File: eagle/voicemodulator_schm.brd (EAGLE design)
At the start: 109 x 84 mm, 33 parts, among them T1 2N5089, T2 2N5089, T3 2N5089, T4 2N5089

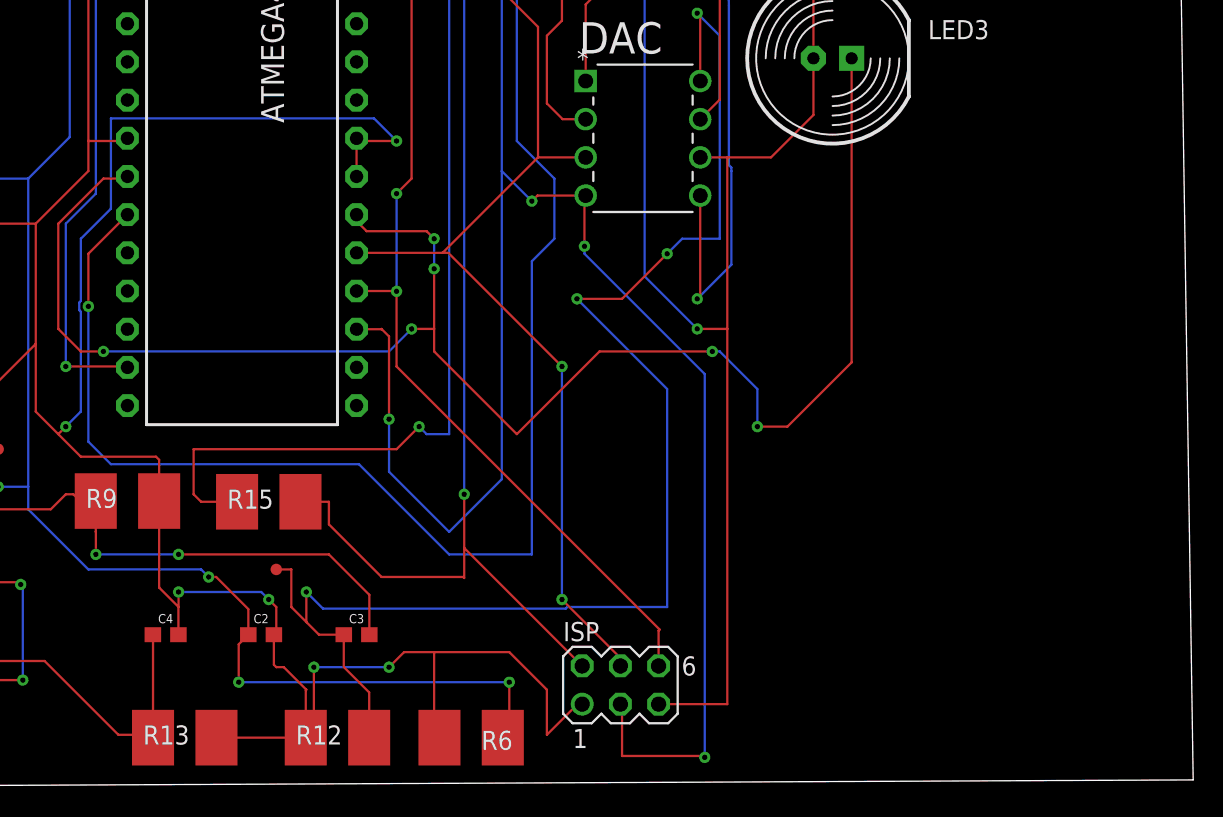
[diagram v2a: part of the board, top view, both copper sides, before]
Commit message: Added output mic jack.
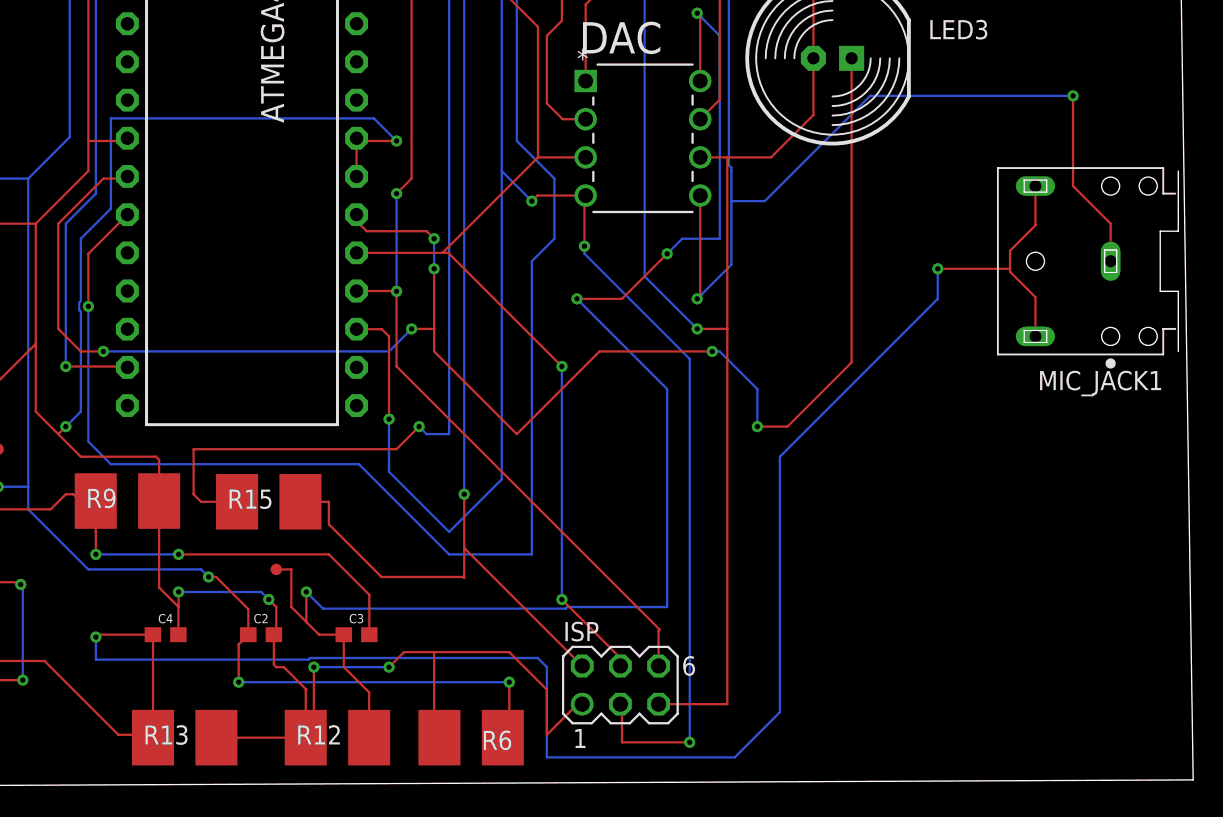
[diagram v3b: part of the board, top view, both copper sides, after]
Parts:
- added MIC_JACK1: SJ1-3523N, SJ1-3523N:CUI_SJ1-3523N
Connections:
- net 0: now also MIC_JACK1.1
- net N$11: now also MIC_JACK1.2, MIC_JACK1.3
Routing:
- net N$11: track 26.9 -> 135.3 mm, vias 0 -> 2
- net 0: track 359.8 -> 397.4 mm, vias 12 -> 13
- net N$16: track 146.3 -> 142.9 mm
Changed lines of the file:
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@@
 <attribute name="VALUE" x="91.35" y="47.23" size="1.27" layer="27"/>
+</element>
+<element name="MIC_JACK1" library="SJ1-3523N" package="CUI_SJ1-3523N" value="SJ1-3523N" x="103.5" y="35" rot="R180">
+<attribute name="MANUFACTURER" value="CUI" x="103.5" y="35" size="1.778" layer="27" rot="R180" display="off"/>
+<attribute name="NAME" x="107.001409375" y="27.69706875" size="1.270509375" layer="25" rot="R180"/>
+<attribute name="PARTREV" value="1.02" x="103.5" y="35" size="1.778" layer="27" rot="R180" display="off"/>
+<attribute name="STANDARD" value="Manufacturer recommendation" x="103.5" y="35" size="1.778" layer="27" rot="R180" display="off"/>
+<attribute name="VALUE" x="107.00286875" y="42.005740625" size="1.271040625" layer="27" rot="R180" align="top-left"/>
 </element>
 </elements>
@@
 <wire x1="78.106771875" y1="41.393228125" x2="78.270515625" y2="41.229484375" width="0.1524" layer="16"/>
 <wire x1="78.270515625" y1="41.229484375" x2="78.274059375" y2="40.9965625" width="0.1524" layer="16"/>
-<wire x1="78.274059375" y1="40.9965625" x2="78.274059375" y2="34.774059375" width="0.1524" layer="16"/>
+<wire x1="78.274059375" y1="40.9965625" x2="78.274059375" y2="39" width="0.1524" layer="16"/>
+<wire x1="78.274059375" y1="39" x2="78.274059375" y2="34.774059375" width="0.1524" layer="16"/>
 <wire x1="78.274059375" y1="34.774059375" x2="76" y2="32.5" width="0.1524" layer="16"/>
 <via x="76" y="32.5" extent="1-16" drill="0.35"/>
@@
 <wire x1="55.5" y1="8" x2="56.5" y2="9" width="0.1524" layer="1"/>
 <wire x1="56.5" y1="9" x2="58.5" y2="9" width="0.1524" layer="1"/>
+<contactref element="MIC_JACK1" pad="1"/>
+<wire x1="103.5" y1="35" x2="103.5" y2="37.5" width="0.1524" layer="1"/>
+<wire x1="101" y1="40" x2="101" y2="46" width="0.1524" layer="1"/>
+<wire x1="103.5" y1="37.5" x2="101" y2="40" width="0.1524" layer="1"/>
+<via x="101" y="46" extent="1-16" drill="0.35"/>
+<wire x1="101" y1="46" x2="87.5" y2="46" width="0.1524" layer="16"/>
+<wire x1="87.5" y1="46" x2="80.5" y2="39" width="0.1524" layer="16"/>
+<wire x1="80.5" y1="39" x2="78.274059375" y2="39" width="0.1524" layer="16"/>
 </signal>
 <signal name="N$1">
@@
 <wire x1="37.5" y1="3.5" x2="39.8018" y2="3.5" width="0.1524" layer="1"/>
 <wire x1="32.59" y1="8.41" x2="37.5" y2="3.5" width="0.1524" layer="1"/>
+<contactref element="MIC_JACK1" pad="3"/>
+<contactref element="MIC_JACK1" pad="2"/>
+<wire x1="96.8078" y1="34.2990625" x2="96.8078" y2="34.5" width="0.1524" layer="1"/>
+<wire x1="96.8078" y1="34.5" x2="96.8078" y2="35.7009375" width="0.1524" layer="1"/>
+<wire x1="98.5" y1="30" x2="98.5" y2="32.6068625" width="0.1524" layer="1"/>
+<wire x1="98.5" y1="37.3931375" x2="98.5" y2="40" width="0.1524" layer="1"/>
+<wire x1="98.5" y1="32.6068625" x2="96.8078" y2="34.2990625" width="0.1524" layer="1"/>
+<wire x1="96.8078" y1="35.7009375" x2="98.5" y2="37.3931375" width="0.1524" layer="1"/>
+<wire x1="39.79" y1="10.16" x2="36.16" y2="10.16" width="0.1524" layer="1"/>
+<wire x1="36.16" y1="10.16" x2="36" y2="10" width="0.1524" layer="1"/>
+<via x="36" y="10" extent="1-16" drill="0.35"/>
+<wire x1="36" y1="10" x2="36" y2="8.5" width="0.1524" layer="16"/>
+<wire x1="36" y1="8.5" x2="50.14185" y2="8.5" width="0.1524" layer="16"/>
+<wire x1="50.14185" y1="8.5" x2="50.24865" y2="8.6068" width="0.1524" layer="16"/>
+<wire x1="50.24865" y1="8.6068" x2="65.3932" y2="8.6068" width="0.1524" layer="16"/>
+<wire x1="65.3932" y1="8.6068" x2="66" y2="8" width="0.1524" layer="16"/>
+<wire x1="66" y1="8" x2="66" y2="2" width="0.1524" layer="16"/>
+<wire x1="66" y1="2" x2="78.5" y2="2" width="0.1524" layer="16"/>
+<wire x1="78.5" y1="2" x2="81.5" y2="5" width="0.1524" layer="16"/>
+<wire x1="81.5" y1="5" x2="81.5" y2="22" width="0.1524" layer="16"/>
+<wire x1="81.5" y1="22" x2="92" y2="32.5" width="0.1524" layer="16"/>
+<wire x1="92" y1="32.5" x2="92" y2="34.5" width="0.1524" layer="16"/>
+<via x="92" y="34.5" extent="1-16" drill="0.35"/>
+<wire x1="92" y1="34.5" x2="96.8078" y2="34.5" width="0.1524" layer="1"/>
 </signal>
 <signal name="N$12">
@@
 <wire x1="65.37" y1="39.37" x2="65" y2="39" width="0.1524" layer="1"/>
 <wire x1="71" y1="5.43" x2="70.89" y2="5.54" width="0.1524" layer="1"/>
-<wire x1="71" y1="5.43" x2="71" y2="2.0922" width="0.1524" layer="1"/>
-<wire x1="76.5" y1="2" x2="76.4078" y2="2.0922" width="0.1524" layer="1"/>
-<wire x1="76.4078" y1="2.0922" x2="71" y2="2.0922" width="0.1524" layer="1"/>
-<via x="76.5" y="2" extent="1-16" drill="0.35"/>
-<wire x1="76.5" y1="27.5" x2="76.5" y2="2" width="0.1524" layer="16"/>
-<wire x1="76.5" y1="27.5" x2="68.5" y2="35.5" width="0.1524" layer="16"/>
+<wire x1="71" y1="5.43" x2="71" y2="3" width="0.1524" layer="1"/>
+<wire x1="75.5" y1="28.5" x2="75.5" y2="3" width="0.1524" layer="16"/>
+<wire x1="75.5" y1="28.5" x2="68.5" y2="35.5" width="0.1524" layer="16"/>
 <wire x1="68.5" y1="35.5" x2="68.5" y2="36" width="0.1524" layer="16"/>
 <via x="68.5" y="36" extent="1-16" drill="0.35"/>
@@
 <wire x1="55" y1="30.5" x2="54.98" y2="30.48" width="0.1524" layer="1"/>
 <wire x1="54.98" y1="30.48" x2="53.34" y2="30.48" width="0.1524" layer="1"/>
+<via x="75.5" y="3" extent="1-16" drill="0.35"/>
+<wire x1="75.5" y1="3" x2="71" y2="3" width="0.1524" layer="1"/>
 </signal>
 <signal name="N$17">

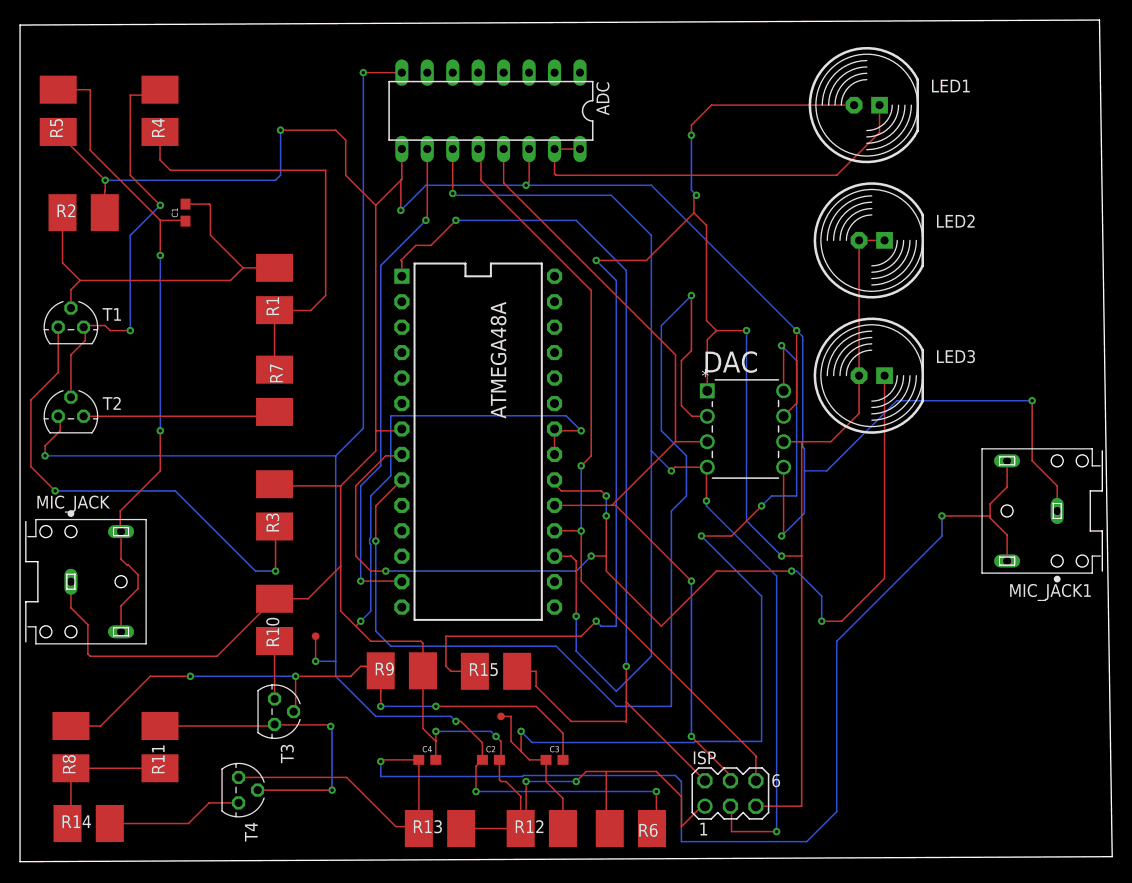
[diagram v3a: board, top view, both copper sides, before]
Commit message: Fix incorrect dimensions in eagle library for DIP
48A DIP device dimensions on layout were incorrect and needed modifying
to match what is specified in the datasheet.
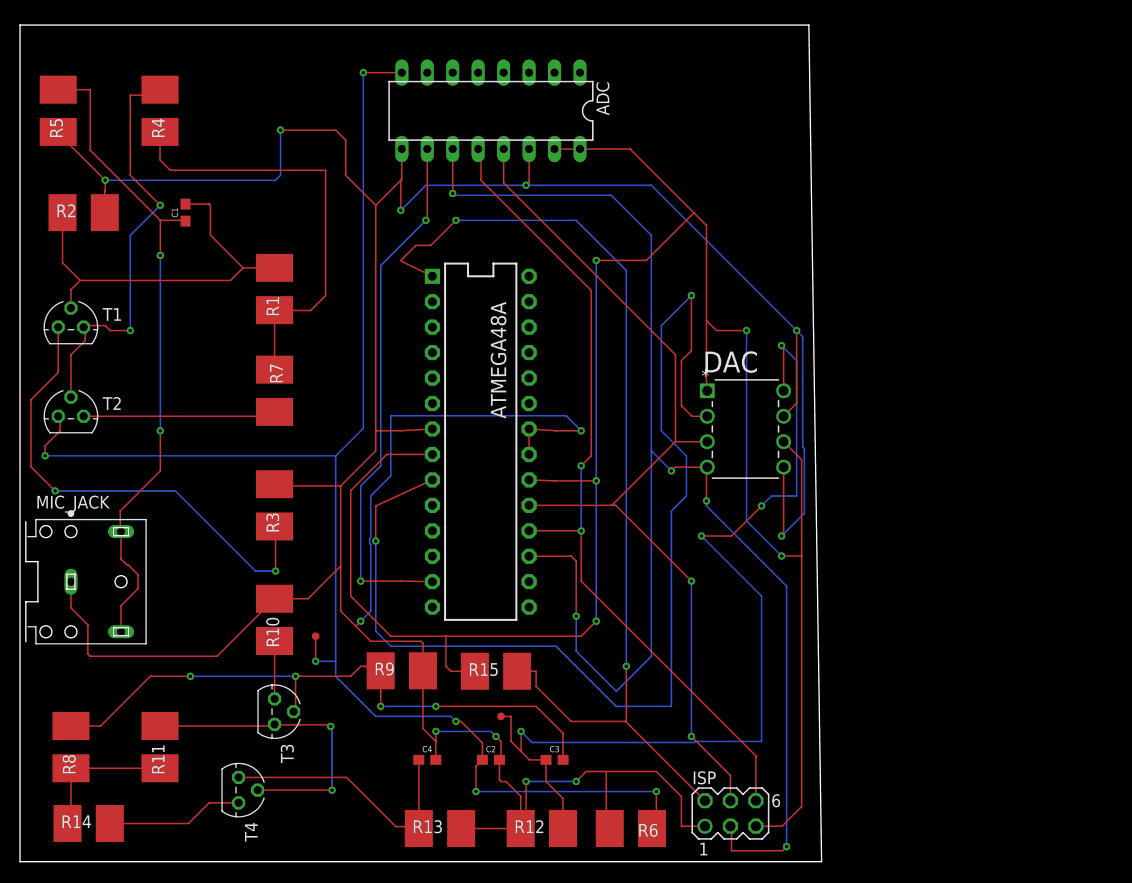
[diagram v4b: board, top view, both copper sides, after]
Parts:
- removed LED1, LED2, LED3: (no value), led:LED10MM
- removed MIC_JACK1: SJ1-3523N, SJ1-3523N:CUI_SJ1-3523N
- moved ISP 2.00 mm to (70.9, 4.81)
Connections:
- removed net N$18: ADC.VDD, ADC.VREF, LED1.K
- removed net N$21: ATMEGA48A.20, ATMEGA48A.8, LED3.K
- net 0: no longer MIC_JACK1.1
- net N$11: no longer MIC_JACK1.2, MIC_JACK1.3
- net VCC: now also ADC.VDD, ADC.VREF, ATMEGA48A.20, ATMEGA48A.8; no longer LED1.A, LED2.A, LED2.K, LED3.A
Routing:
- net N$21: track 110.6 -> 0.00 mm, vias 6 -> 0
- net N$11: track 135.3 -> 26.9 mm, vias 2 -> 0
- net N$18: track 42.0 -> 0.00 mm
- net 0: track 397.4 -> 364.4 mm, vias 13 -> 12
- net N$16: track 142.9 -> 148.4 mm
- net N$2: track 78.1 -> 82.6 mm
- net N$17: track 86.8 -> 91.3 mm
- net N$19: track 50.0 -> 53.0 mm
- net N$20: track 107.1 -> 109.7 mm
- net N$22: track 97.9 -> 99.8 mm
- net VCC: track 216.6 -> 215.2 mm, vias 6 -> 5
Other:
- board size 109 x 84 mm -> 80 x 83.5 mm

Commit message: Segmented output into two paths with 0 ohm resistors
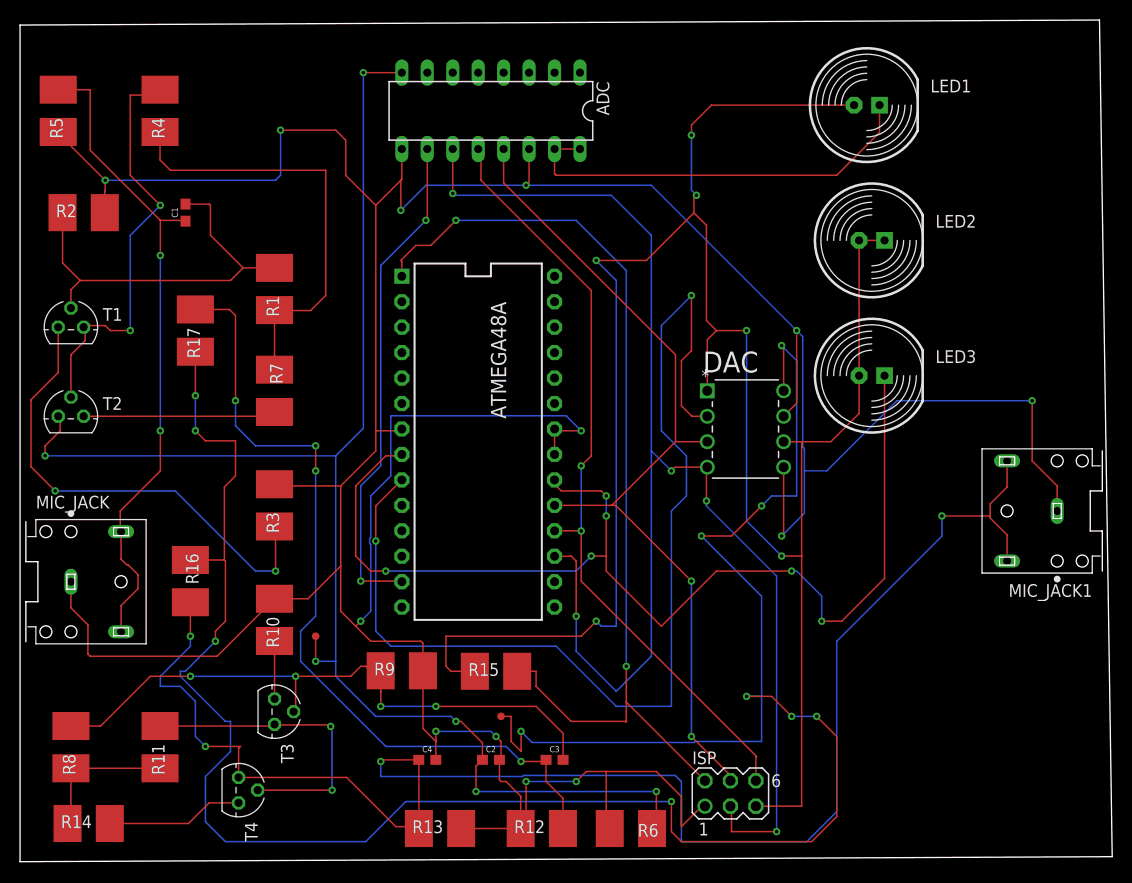
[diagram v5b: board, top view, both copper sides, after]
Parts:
- added LED1, LED2, LED3: (no value), led:LED10MM
- added MIC_JACK1: SJ1-3523N, SJ1-3523N:CUI_SJ1-3523N
- added R16, R17: (no value), resistor-shunt:SMS-WAV
- moved ISP 2.00 mm to (70.9, 6.81)
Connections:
- new net N$18: ADC.VDD, ADC.VREF, LED1.K
- new net N$21: ATMEGA48A.20, ATMEGA48A.8, LED3.K
- new net N$23: C3.1, R12.1, R17.1
- net 0: now also MIC_JACK1.1
- net N$11: now also MIC_JACK1.2, MIC_JACK1.3, R16.1
- net N$4: now also R16.2, R17.2; no longer C3.1, R12.1
- net VCC: now also LED1.A, LED2.A, LED2.K, LED3.A; no longer ADC.VDD, ADC.VREF, ATMEGA48A.20, ATMEGA48A.8
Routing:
- net N$4: track 96.2 -> 235.6 mm, vias 4 -> 11
- net N$11: track 26.9 -> 160.7 mm, vias 0 -> 4
- net N$21: track 0.00 -> 110.6 mm, vias 0 -> 6
- net N$23: track 0.00 -> 82.4 mm, vias 0 -> 4
- net N$18: track 0.00 -> 42.0 mm
- net 0: track 364.4 -> 397.4 mm, vias 12 -> 13
- net N$16: track 148.4 -> 142.9 mm
- net N$2: track 82.6 -> 78.1 mm
- net N$17: track 91.3 -> 86.8 mm
- net N$19: track 53.0 -> 50.0 mm
- net N$20: track 109.7 -> 107.1 mm
- net N$22: track 99.8 -> 97.9 mm
- net VCC: track 215.2 -> 216.6 mm, vias 5 -> 6
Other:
- board size 80 x 83.5 mm -> 109 x 84 mm
